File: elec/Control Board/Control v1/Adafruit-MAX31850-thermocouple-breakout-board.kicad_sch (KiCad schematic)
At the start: 17 parts, among them U1 MAX31850, U2 MIC5225-3.3, X1 3.5mm

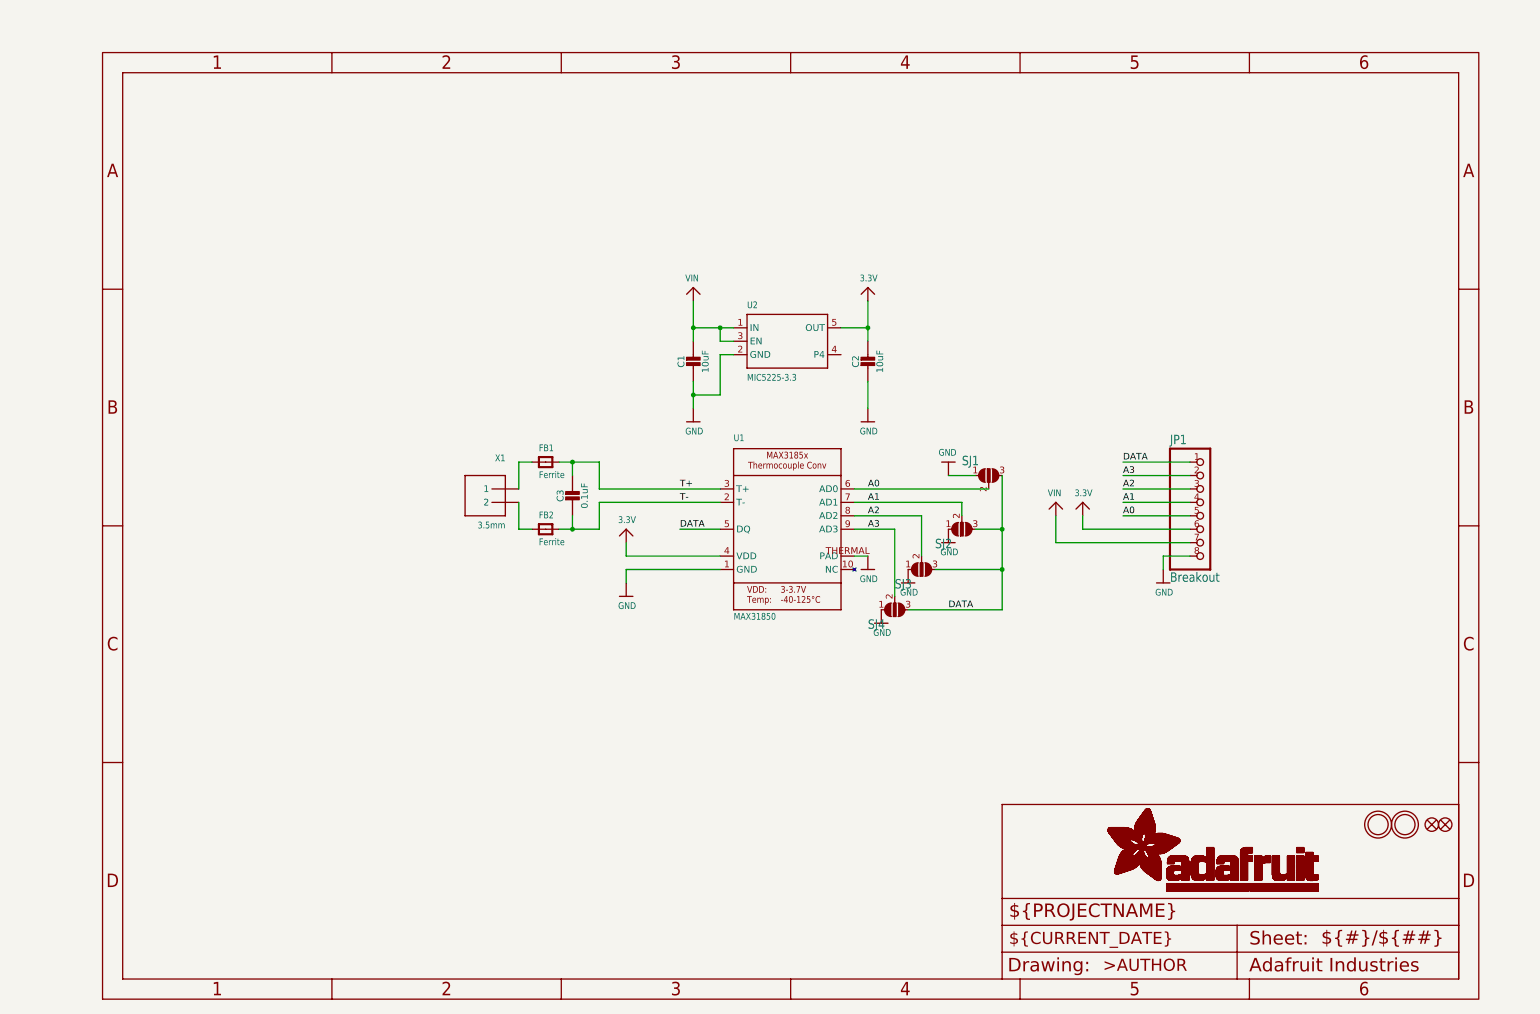
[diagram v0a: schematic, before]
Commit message: added labels for heiarchy sheets, and first pass on basic control interface circuits
Signed-off-by: lokimetasmith <lokimail@gmail.com>
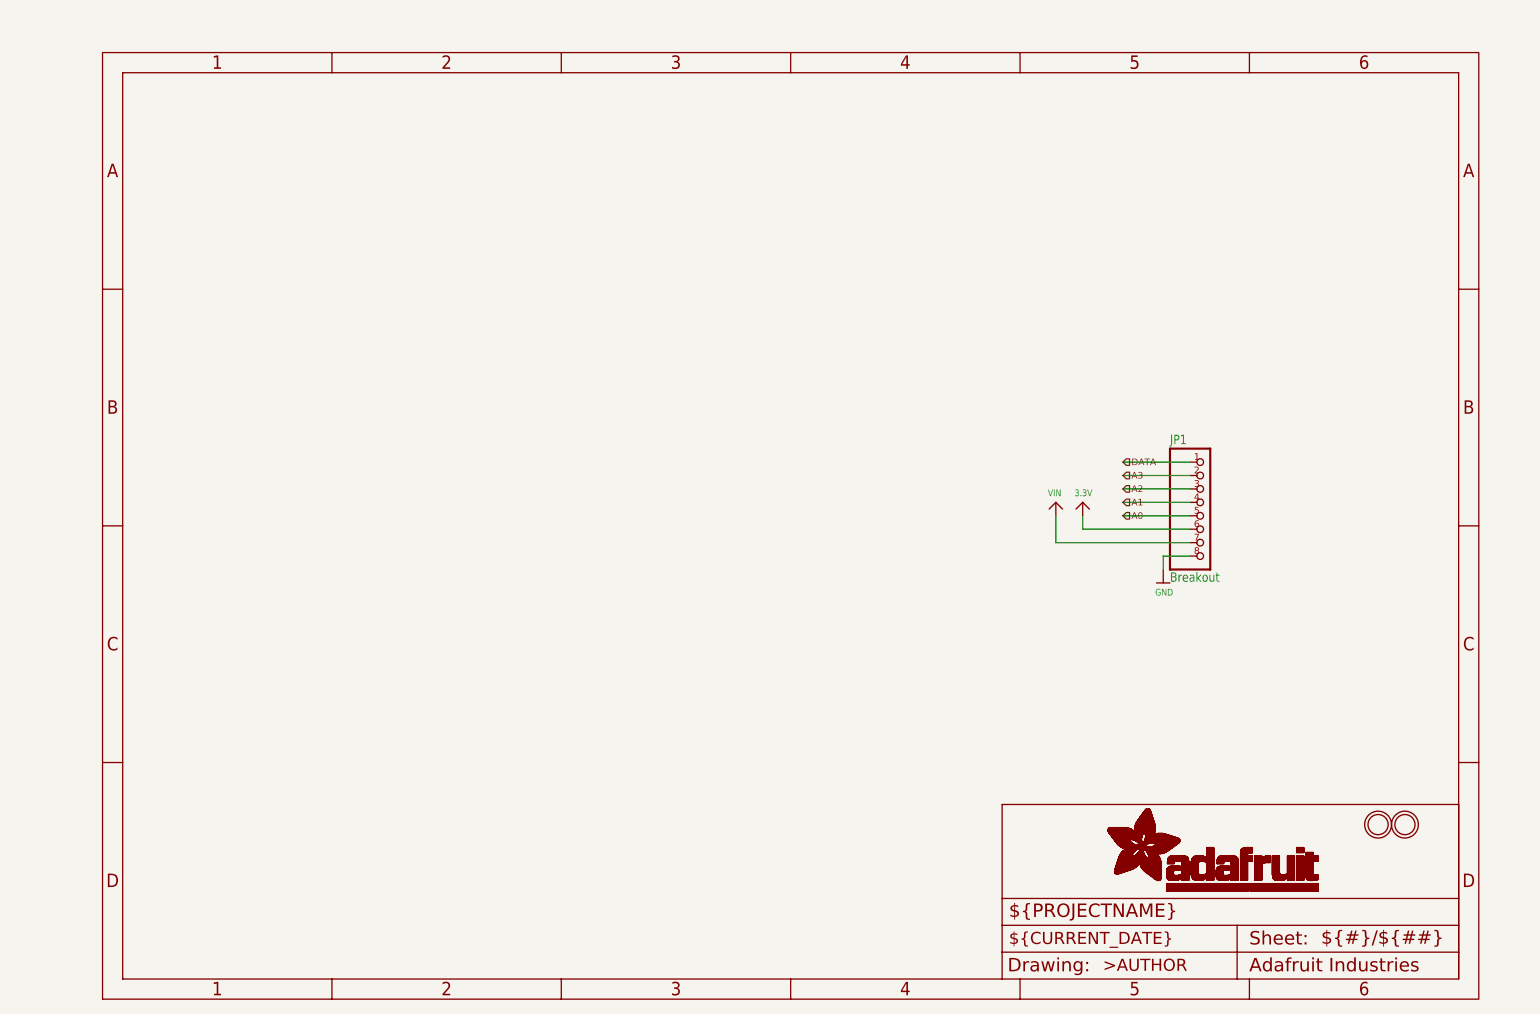
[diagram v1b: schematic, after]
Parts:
- removed C1, C2: 10uF, Control v1:0805-NO, symbol Control v1-eagle-import:microbuilder_CAP_CERAMIC0805-NOOUTLINE
- removed C3: 0.1uF, Control v1:0805-NO, symbol Control v1-eagle-import:microbuilder_CAP_CERAMIC0805-NOOUTLINE
- removed FB1, FB2: Ferrite, Control v1:0805, symbol Control v1-eagle-import:microbuilder_FERRITE0805
- removed FID1, FID2: FIDUCIAL{dblquote}{dblquote}, Control v1:FIDUCIAL_1MM, symbol Control v1-eagle-import:microbuilder_FIDUCIAL{dblquote}{dblquote}
- removed SJ1, SJ2, SJ3, SJ4: SOLDERJUMPER_2WAY, Control v1:SOLDERJUMPER_2WAY_OPEN_NOPASTE, symbol Control v1-eagle-import:microbuilder_SOLDERJUMPER_2WAY
- removed U1: MAX31850, Control v1:TDFN10_3X4MM, symbol Control v1-eagle-import:microbuilder_MAX3185X
- removed U2: MIC5225-3.3, Control v1:SOT23-5, symbol Control v1-eagle-import:microbuilder_VREG_SOT23-5
- removed X1: 3.5mm, Control v1:TERMBLOCK_1X2-3.5MM, symbol Control v1-eagle-import:microbuilder_TERMBLOCK_1X2

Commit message: Add Lees PublicInvention submodule library. Update Control V1 project and schematic for new library.
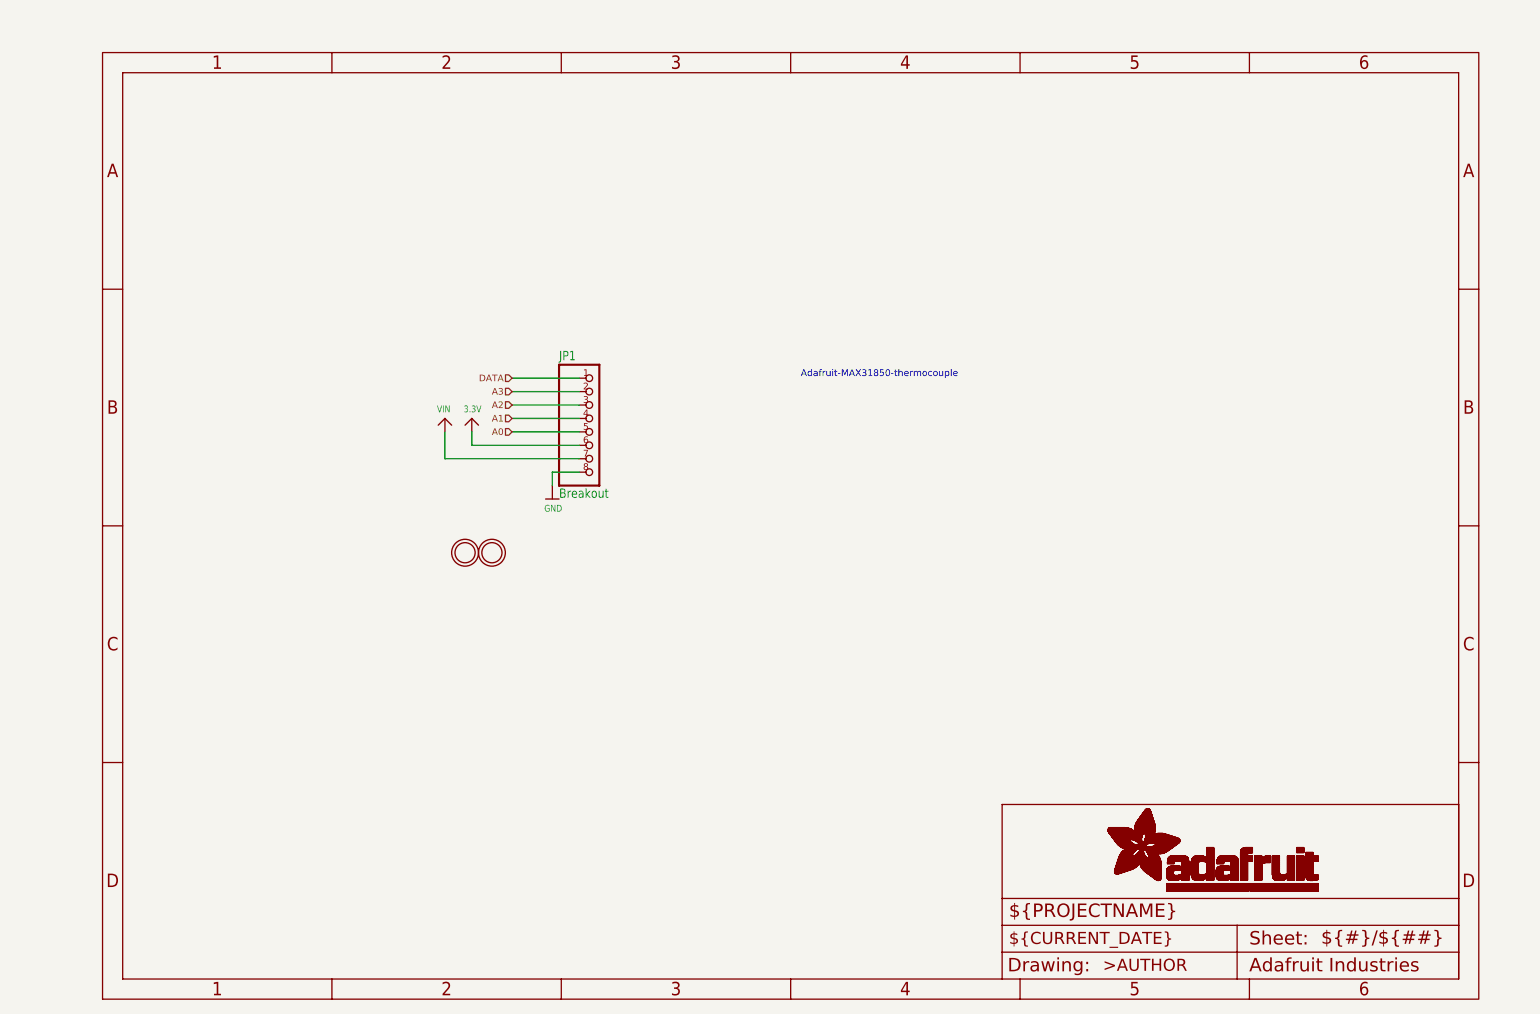
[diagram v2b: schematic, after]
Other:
- note added: "Adafruit-MAX31850-thermocouple"
- moved on the sheet: JP1

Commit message: Add fan circuits. Add thermocouple interface circuits.
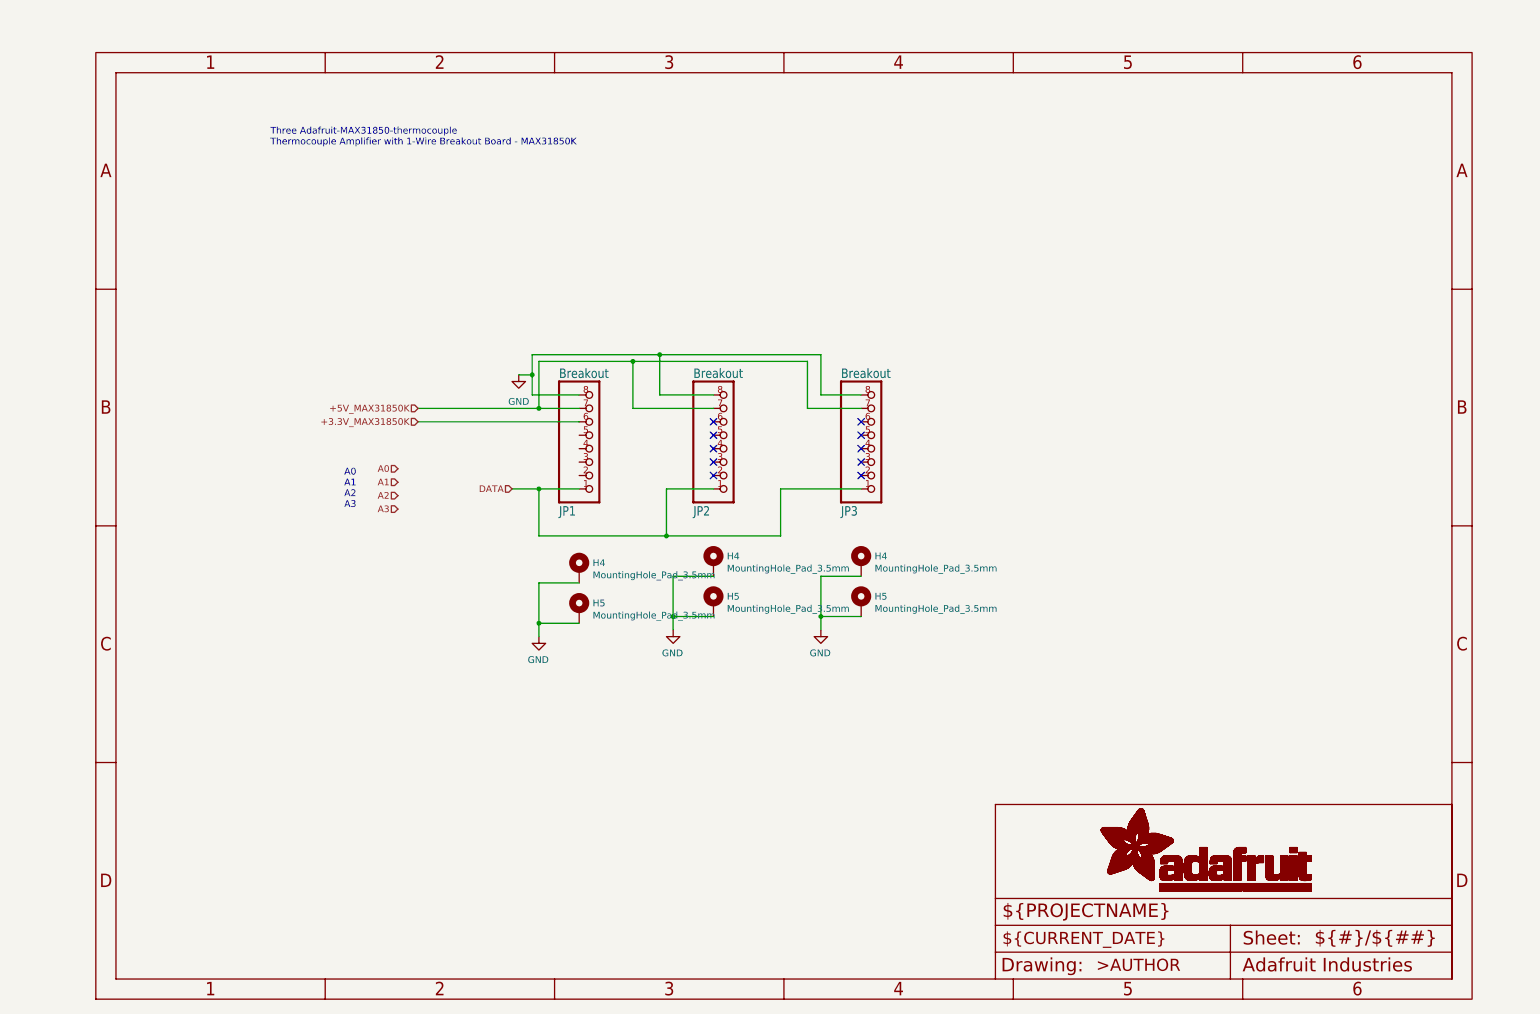
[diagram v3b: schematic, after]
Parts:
- removed U$8, U$9: MOUNTINGHOLE2.5, Control v1:MOUNTINGHOLE_2.5_PLATED, symbol Control v1-eagle-import:microbuilder_MOUNTINGHOLE2.5
- added H4 (x3), H5 (x3): MountingHole_Pad_3.5mm, GeneralPurposeAlarmDevicePCB:MountingHole_3.5mm_Pad_Via, symbol GPAD_SCH_LIB:MountingHole_Pad_3.5mm
- added JP2, JP3: Breakout, Control v1:1X08_ROUND_70, symbol Control v1-eagle-import:microbuilder_HEADER-1X870MIL
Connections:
- net A0: no longer JP1.5
- net A1: no longer JP1.4
- net A2: no longer JP1.3
- net A3: no longer JP1.2
- net DATA: now also JP2.1, JP3.1
- net GND: now also H4.1, H4.1, H4.1, H5.1, H5.1, H5.1, JP2.8, JP3.8
- net 3.3V renamed +3.3V_MAX31850K
- net VIN renamed +5V_MAX31850K
- net +5V_MAX31850K: now also JP2.7, JP3.7
- no-connect marks 0 -> 10
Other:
- note added: "A0 A1 A2 A3"
- note added: "Three Adafruit-MAX31850-thermocouple Thermocouple Amplifier with 1-Wire Breakout Board - MAX31850K"
- note removed: "Adafruit-MAX31850-thermocouple"
- moved on the sheet: JP1

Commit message: Move some components for rough placement.
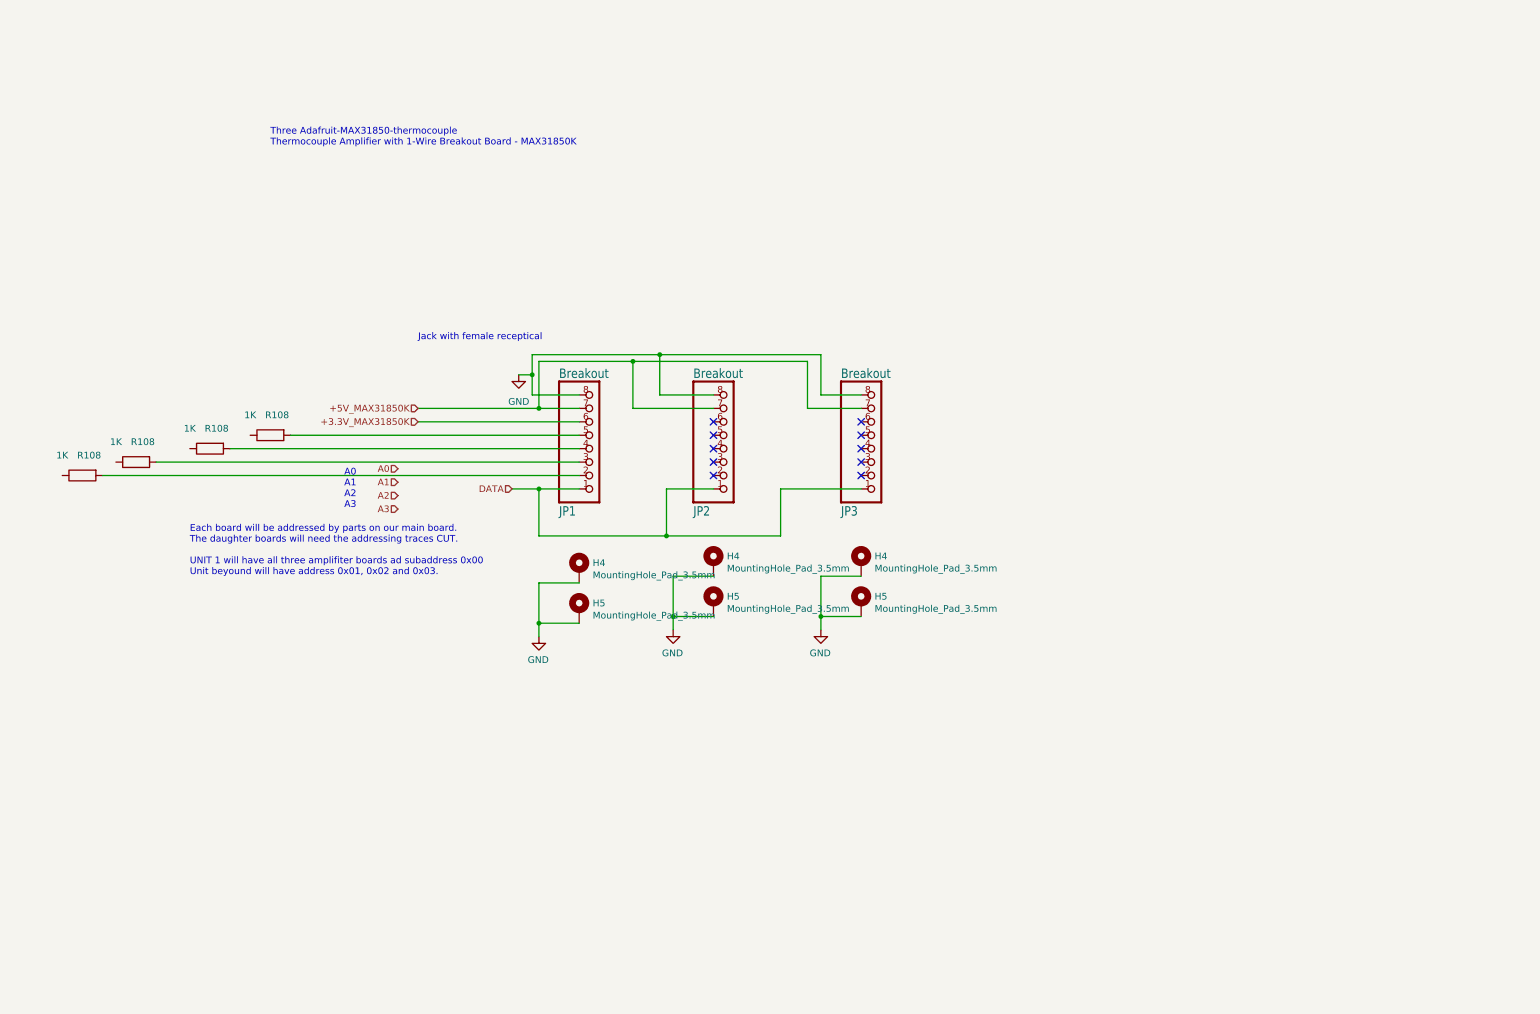
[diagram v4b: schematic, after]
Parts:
- added R108 (x4): 1K, Resistor_SMD:R_0603_1608Metric_Pad0.98x0.95mm_HandSolder, symbol Device:R
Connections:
- net at JP1.2: now also R108.2
- net at JP1.3: now also R108.2
- net at JP1.4: now also R108.2
- net at JP1.5: now also R108.2
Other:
- note added: "Each board will be addressed by parts on our main board. The daughter boards will need the addressing traces CUT. UNIT 1 will have all three amplifiter boards ad subaddress 0x00 Unit beyound will have address 0x01, 0x02 and 0x03."
- note added: "Jack with female receptical"
